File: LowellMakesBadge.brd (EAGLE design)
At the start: 51.9 x 52 mm, 2 parts

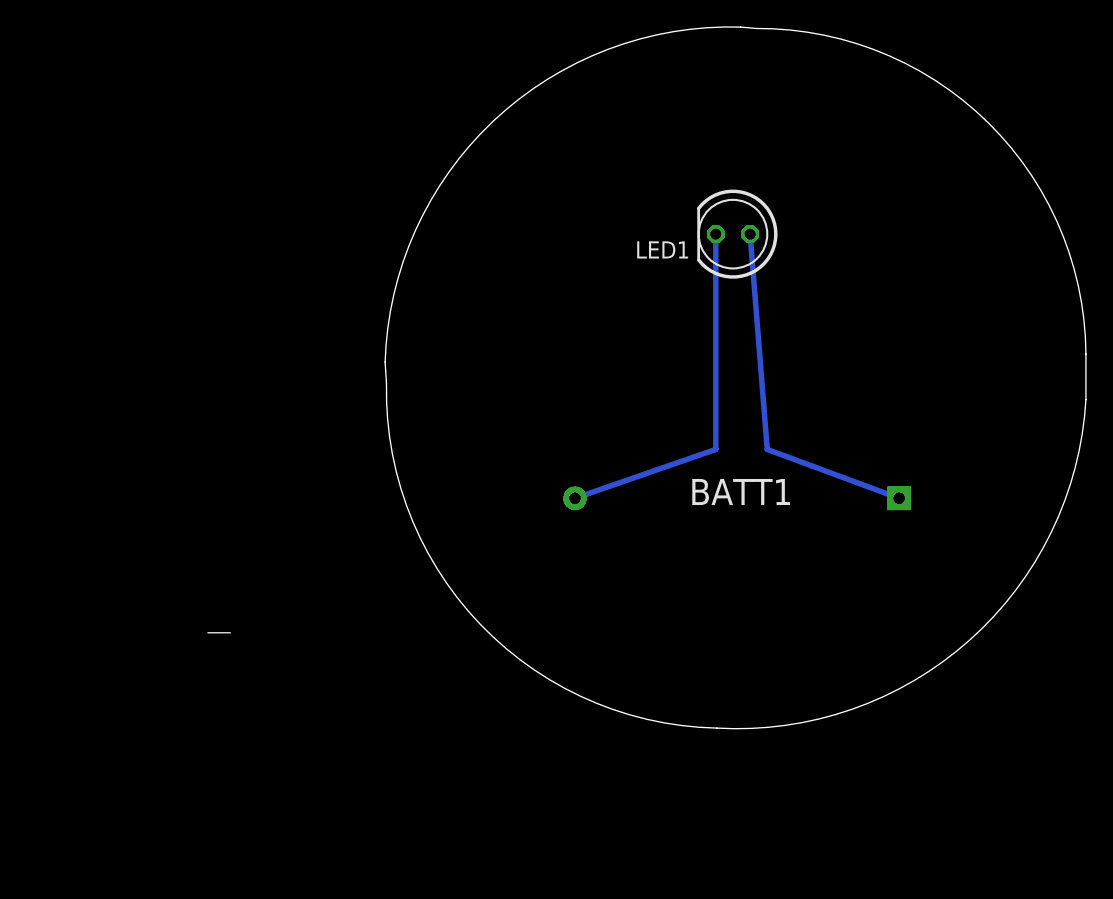
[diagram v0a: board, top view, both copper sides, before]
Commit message: Created Very Simple First Version.  Should put copper text with version on the back
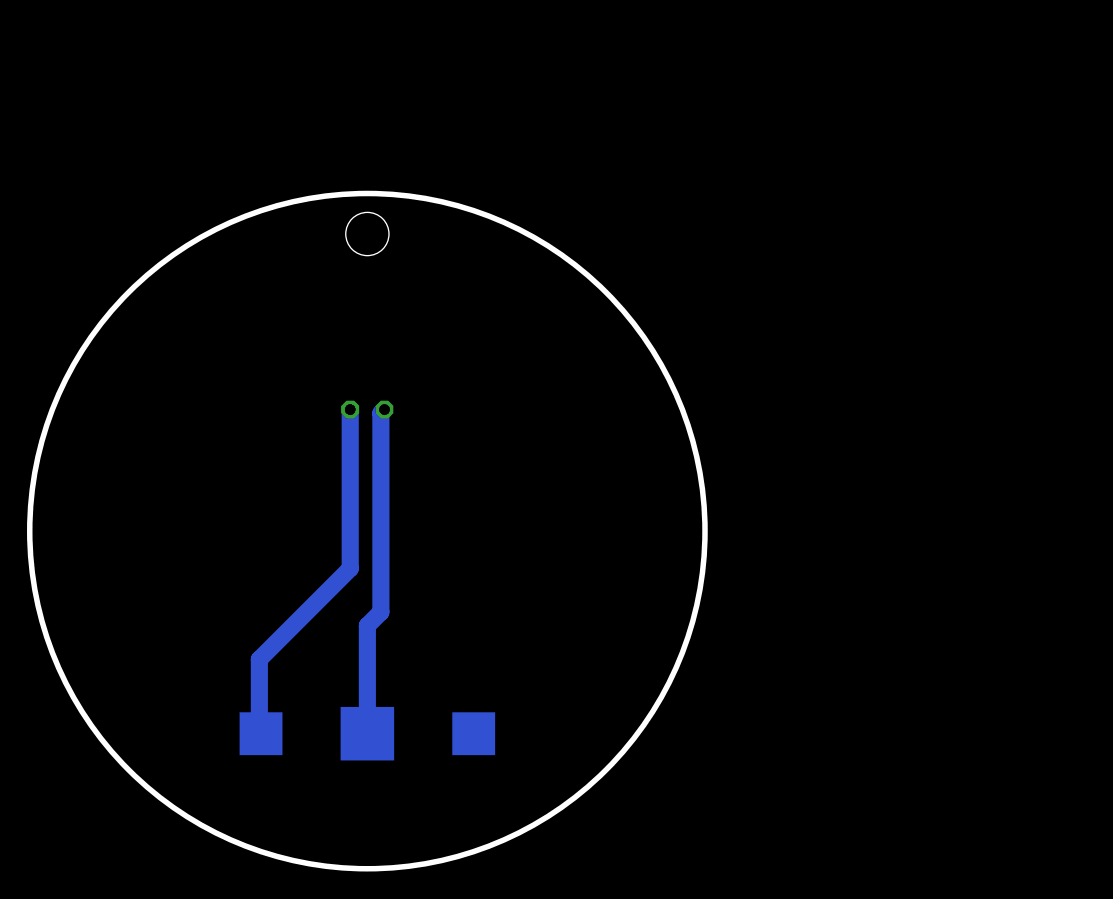
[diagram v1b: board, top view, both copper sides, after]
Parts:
- removed BATT1: FKIT-COIN_CELLLIR2450-H, SparkFun-Electromechanical:FKIT-LIR2450-H
- added BAT1: (no value), SparkFun:BATTCON_12MM
- added U$1: (no value), LowellMakesEagleLibrary:LOWELLMAKES-LOGO2
- moved LED1 30.0 mm to (25.0, 34.0), flipped to the bottom
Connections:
- net GND: now also BAT1.GND; no longer BATT1.NEG
- net N$1: now also BAT1.PWR@1; no longer BATT1.POS
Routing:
- net GND: track 27.0 -> 24.5 mm
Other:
- board size 51.9 x 52 mm -> 50 x 50 mm

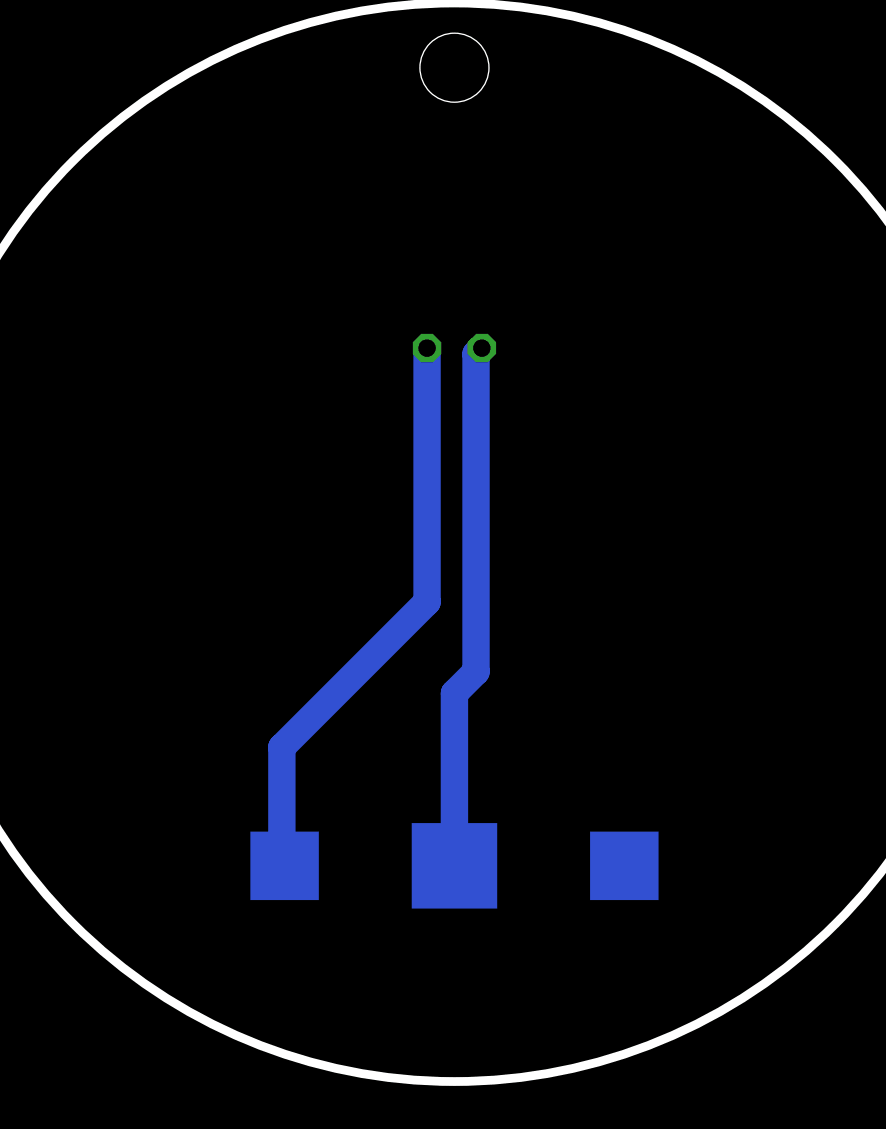
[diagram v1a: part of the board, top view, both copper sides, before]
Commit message: Updated battery to be through hole and added text.  Need to add stop
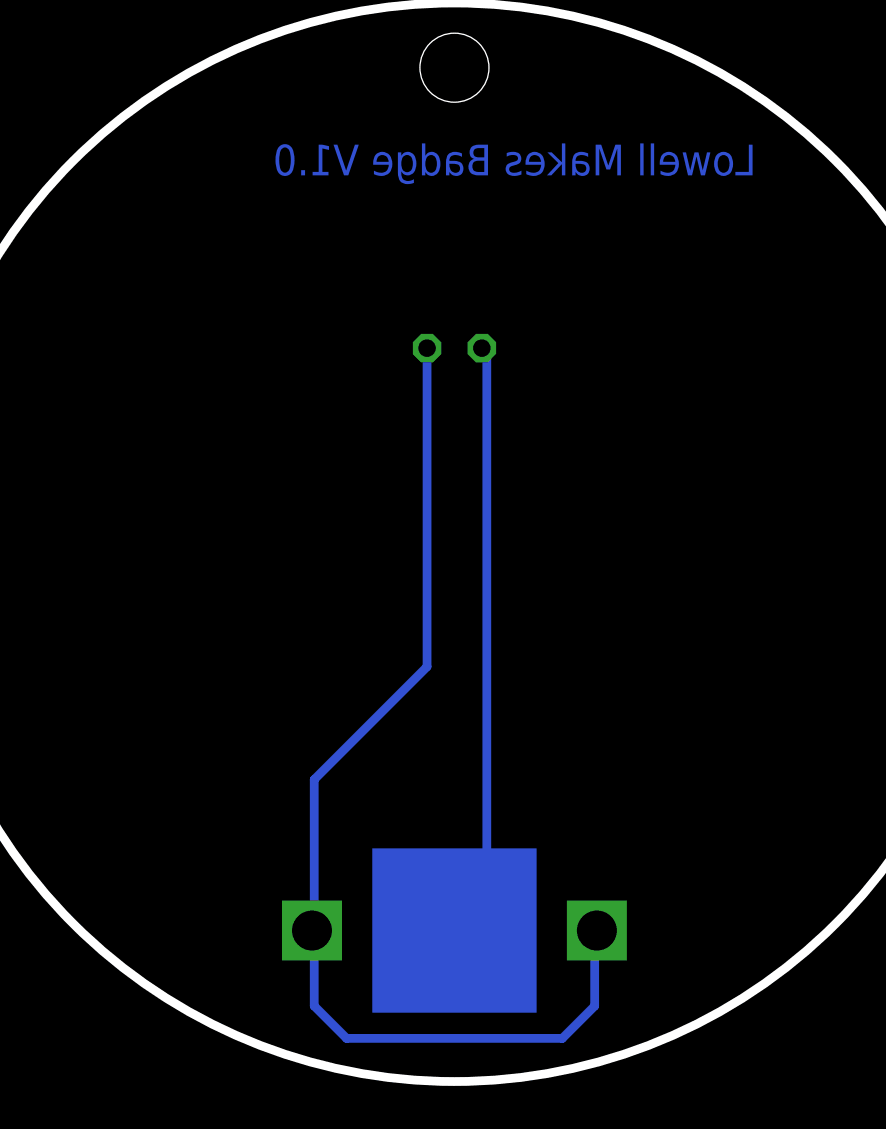
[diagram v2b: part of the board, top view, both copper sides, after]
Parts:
- BAT1: device SparkFun:BATTCON_12MM -> SparkFun:BATTCON_12MM_PTH
- moved BAT1 3.00 mm to (25.0, 7.00)
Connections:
- net N$1: now also BAT1.VCC@1; no longer BAT1.PWR@1
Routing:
- net N$2: track 0.00 -> 21.2 mm
- net GND: track 24.5 -> 28.7 mm
- net N$1: track 26.8 -> 29.2 mm
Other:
- board text added: "Lowell Makes Badge V1.0"
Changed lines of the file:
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@@
 <setting verticaltext="up"/>
 </settings>
-<grid distance="0.5" unitdist="mm" unit="mm" style="lines" multiple="1" display="yes" altdistance="0.025" altunitdist="inch" altunit="inch"/>
+<grid distance="10" unitdist="mil" unit="mil" style="lines" multiple="1" display="yes" altdistance="0.025" altunitdist="inch" altunit="inch"/>
 <layers>
 <layer number="1" name="Top" color="4" fill="1" visible="yes" active="yes"/>
@@
 <circle x="25" y="25" radius="25" width="0.4064" layer="20"/>
 <hole x="25" y="47" drill="3.2"/>
+<text x="38.992" y="42.008" size="1.4224" layer="16" font="vector" ratio="17" rot="MR0">Lowell Makes Badge V1.0</text>
 </plain>
 <attributes>
@@
 </class>
 </classes>
-<designrules name="default">
+<designrules name="SeeedStudio_2layer_DRU_no_angle_20140221">
 <description language="de">&lt;b&gt;EAGLE Design Rules&lt;/b&gt;
 &lt;p&gt;
@@
 necessary adjustments and save your customized
 design rules under a new name.</description>
+<description language="zh">&lt;b&gt;Seeed Studio EAGLE Design Rules&lt;/b&gt;
+</description>
 <param name="layerSetup" value="(1*16)"/>
-<param name="mtCopper" value="0.035mm 0.035mm 0.035mm 0.035mm 0.035mm 0.035mm 0.035mm 0.035mm 0.035mm 0.035mm 0.035mm 0.035mm 0.035mm 0.035mm 0.035mm 0.035mm"/>
-<param name="mtIsolate" value="1.5mm 0.15mm 0.2mm 0.15mm 0.2mm 0.15mm 0.2mm 0.15mm 0.2mm 0.15mm 0.2mm 0.15mm 0.2mm 0.15mm 0.2mm"/>
-<param name="mdWireWire" value="8mil"/>
-<param name="mdWirePad" value="8mil"/>
-<param name="mdWireVia" value="8mil"/>
-<param name="mdPadPad" value="8mil"/>
-<param name="mdPadVia" value="8mil"/>
-<param name="mdViaVia" value="8mil"/>
-<param name="mdSmdPad" value="8mil"/>
-<param name="mdSmdVia" value="8mil"/>
-<param name="mdSmdSmd" value="8mil"/>
+<param name="mtCopper" value="0.035mm 0.0175mm 0.035mm 0.035mm 0.035mm 0.035mm 0.035mm 0.035mm 0.035mm 0.035mm 0.035mm 0.035mm 0.035mm 0.035mm 0.0175mm 0.035mm"/>
+<param name="mtIsolate" value="1.5mm 1.1mm 0.2mm 0.15mm 0.2mm 0.15mm 0.2mm 0.15mm 0.2mm 0.15mm 0.2mm 0.15mm 0.2mm 0.15mm 0.2mm"/>
+<param name="mdWireWire" value="6mil"/>
+<param name="mdWirePad" value="6mil"/>
+<param name="mdWireVia" value="6mil"/>
+<param name="mdPadPad" value="6mil"/>
+<param name="mdPadVia" value="6mil"/>
+<param name="mdViaVia" value="6mil"/>
+<param name="mdSmdPad" value="0mil"/>
+<param name="mdSmdVia" value="0mil"/>
+<param name="mdSmdSmd" value="0mil"/>
 <param name="mdViaViaSameLayer" value="8mil"/>
 <param name="mnLayersViaInSmd" value="2"/>
-<param name="mdCopperDimension" value="40mil"/>
-<param name="mdDrill" value="8mil"/>
+<param name="mdCopperDimension" value="10mil"/>
+<param name="mdDrill" value="10mil"/>
 <param name="mdSmdStop" value="0mil"/>
-<param name="msWidth" value="10mil"/>
-<param name="msDrill" value="24mil"/>
-<param name="msMicroVia" value="9.99mm"/>
+<param name="msWidth" value="6mil"/>
+<param name="msDrill" value="12mil"/>
+<param name="msMicroVia" value="12mil"/>
 <param name="msBlindViaRatio" value="0.5"/>
 <param name="rvPadTop" value="0.25"/>
@@
 <param name="rlMinPadBottom" value="10mil"/>
 <param name="rlMaxPadBottom" value="20mil"/>
-<param name="rlMinViaOuter" value="8mil"/>
+<param name="rlMinViaOuter" value="6mil"/>
 <param name="rlMaxViaOuter" value="20mil"/>
-<param name="rlMinViaInner" value="8mil"/>
+<param name="rlMinViaInner" value="6mil"/>
 <param name="rlMaxViaInner" value="20mil"/>
 <param name="rlMinMicroViaOuter" value="4mil"/>
@@
 <param name="psTop" value="-1"/>
 <param name="psBottom" value="-1"/>
-<param name="psFirst" value="-1"/>
+<param name="psFirst" value="0"/>
 <param name="psElongationLong" value="100"/>
 <param name="psElongationOffset" value="100"/>
 <param name="mvStopFrame" value="1"/>
 <param name="mvCreamFrame" value="0"/>
-<param name="mlMinStopFrame" value="4mil"/>
-<param name="mlMaxStopFrame" value="4mil"/>
+<param name="mlMinStopFrame" value="2mil"/>
+<param name="mlMaxStopFrame" value="2mil"/>
 <param name="mlMinCreamFrame" value="0mil"/>
 <param name="mlMaxCreamFrame" value="0mil"/>
-<param name="mlViaStopLimit" value="0mil"/>
+<param name="mlViaStopLimit" value="100mil"/>
 <param name="srRoundness" value="0"/>
 <param name="srMinRoundness" value="0mil"/>
@@
 <param name="checkAngle" value="0"/>
 <param name="checkFont" value="1"/>
-<param name="checkRestrict" value="1"/>
+<param name="checkRestrict" value="0"/>
 <param name="useDiameter" value="13"/>
 <param name="maxErrors" value="50"/>
@@
 <elements>
 <element name="LED1" library="led" package="LED5MM" value="" x="25" y="34" rot="MR180"/>
-<element name="BAT1" library="SparkFun" package="BATTCON_12MM" value="" x="25" y="10" rot="MR180"/>
 <element name="U$1" library="LowellMakesEagleLibrary" package="LOWELLMAKES-LOGO2" value="" x="2" y="8.5"/>
+<element name="BAT1" library="SparkFun" package="BATTCON_12MM_PTH" value="" x="25" y="7" smashed="yes" rot="MR180">
+<attribute name="NAME" x="16.364" y="4.714" size="0.4064" layer="26" rot="MR180"/>
+<attribute name="VALUE" x="21.19" y="12.08" size="0.4064" layer="28" rot="MR180"/>
+</element>
 </elements>
 <signals>
 <signal name="N$1">
 <contactref element="LED1" pad="A"/>
-<contactref element="BAT1" pad="PWR@1"/>
-<wire x1="23.73" y1="34" x2="23.73" y2="22.23" width="1.27" layer="16"/>
-<wire x1="23.73" y1="22.23" x2="17" y2="15.5" width="1.27" layer="16"/>
-<wire x1="17" y1="15.5" x2="17" y2="10.126" width="1.27" layer="16"/>
-<wire x1="17" y1="10.126" x2="17.126" y2="10" width="1.27" layer="16"/>
+<contactref element="BAT1" pad="VCC@1"/>
+<wire x1="23.73" y1="34" x2="23.73" y2="19.23" width="0.4064" layer="16"/>
+<wire x1="23.73" y1="19.23" x2="18.5" y2="14" width="0.4064" layer="16"/>
+<wire x1="18.5" y1="14" x2="18.5" y2="7.104" width="0.4064" layer="16"/>
+<wire x1="18.5" y1="7.104" x2="18.396" y2="7" width="0.4064" layer="16"/>
 </signal>
 <signal name="GND">
 <contactref element="LED1" pad="K"/>
 <contactref element="BAT1" pad="GND"/>
-<wire x1="25" y1="10" x2="25" y2="18" width="1.27" layer="16"/>
-<wire x1="25" y1="18" x2="26" y2="19" width="1.27" layer="16"/>
-<wire x1="26" y1="19" x2="26" y2="33.73" width="1.27" layer="16"/>
-<wire x1="26" y1="33.73" x2="26.27" y2="34" width="1.27" layer="16"/>
+<wire x1="26.27" y1="34" x2="26.5" y2="34" width="0.4064" layer="16"/>
+<wire x1="26.5" y1="34" x2="26.5" y2="9" width="0.4064" layer="16"/>
+<wire x1="26.5" y1="9" x2="25" y2="9" width="0.4064" layer="16"/>
+<wire x1="25" y1="9" x2="25" y2="7" width="0.4064" layer="16"/>
+</signal>
+<signal name="N$2">
+<wire x1="18.5" y1="7" x2="18.5" y2="3.5" width="0.4064" layer="16"/>
+<wire x1="18.5" y1="3.5" x2="20" y2="2" width="0.4064" layer="16"/>
+<wire x1="20" y1="2" x2="30" y2="2" width="0.4064" layer="16"/>
+<wire x1="30" y1="2" x2="31.5" y2="3.5" width="0.4064" layer="16"/>
+<wire x1="31.5" y1="3.5" x2="31.5" y2="7" width="0.4064" layer="16"/>
 </signal>
 </signals>
